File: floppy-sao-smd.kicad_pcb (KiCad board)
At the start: 2 copper layers, 41.5 x 43.6 mm, 13 parts, among them U1 M24C02-WMN, U2 AT24C256C, X1 Badgelife_sao_connector_v169b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

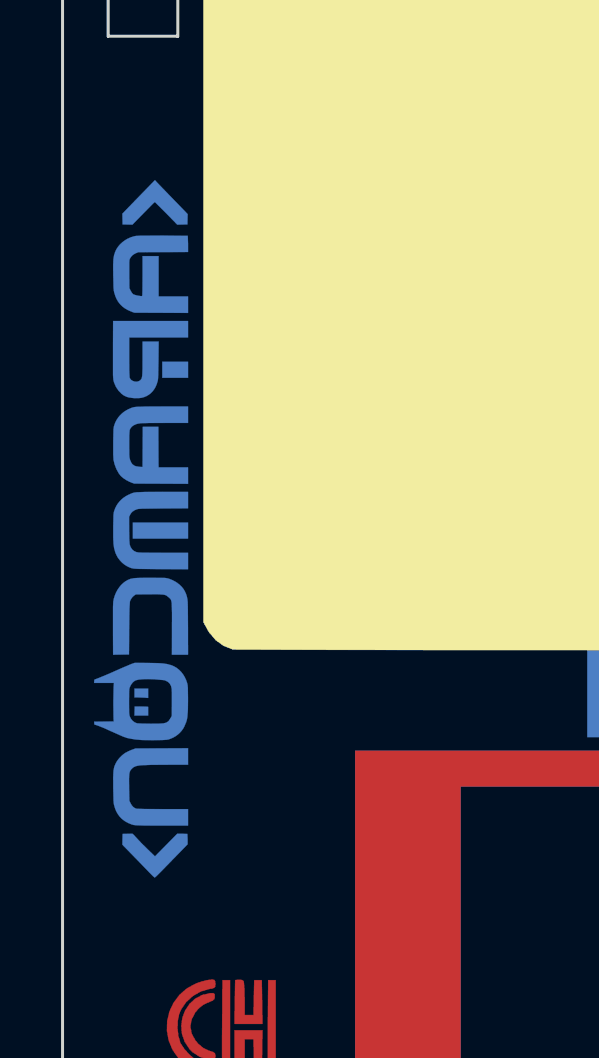
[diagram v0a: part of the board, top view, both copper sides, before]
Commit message: feat: replace conference logo with Wokwi logo
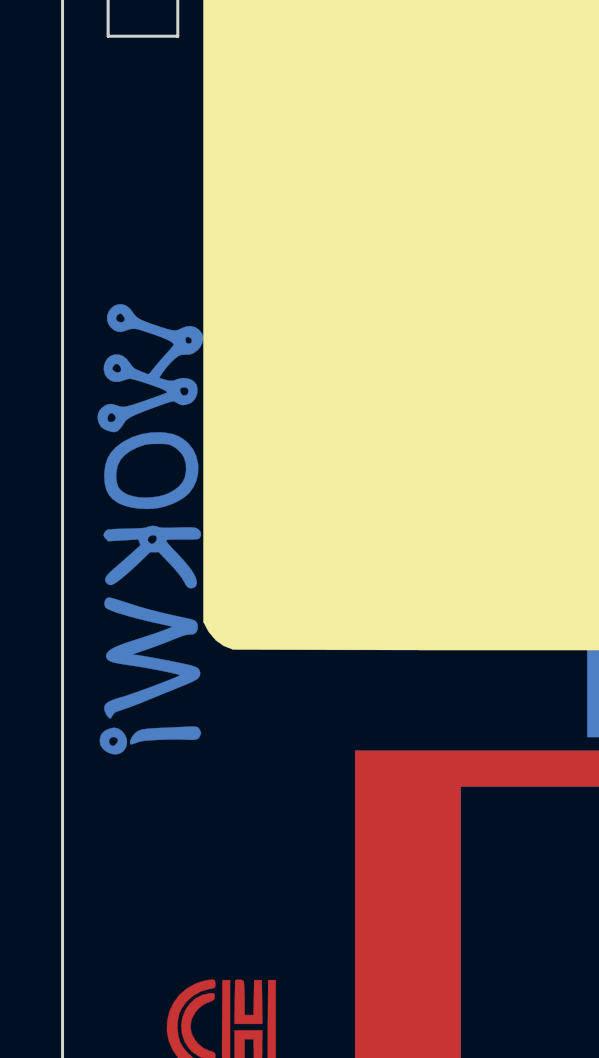
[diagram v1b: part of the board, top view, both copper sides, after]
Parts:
- logo1: renamed from svg2mod; footprint floppy:aramcon-logo-cu -> floppy:wokwi-cu
- moved logo1 0.30 mm to (132.2, 104.7)
